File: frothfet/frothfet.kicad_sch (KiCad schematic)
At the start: 8 parts

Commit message: bom and placement all check out.  ready for production!
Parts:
- H1, H2, H3, H4: now left out of the parts list
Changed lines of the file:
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@@
 		(unit 1)
 		(exclude_from_sim no)
-		(in_bom yes)
+		(in_bom no)
 		(on_board yes)
 		(dnp no)
@@
 		(unit 1)
 		(exclude_from_sim no)
-		(in_bom yes)
+		(in_bom no)
 		(on_board yes)
 		(dnp no)
@@
 		(unit 1)
 		(exclude_from_sim no)
-		(in_bom yes)
+		(in_bom no)
 		(on_board yes)
 		(dnp no)
@@
 		(unit 1)
 		(exclude_from_sim no)
-		(in_bom yes)
-		(on_board yes)
-		(dnp no)
+		(in_bom no)
+		(on_board yes)
+		(dnp no)

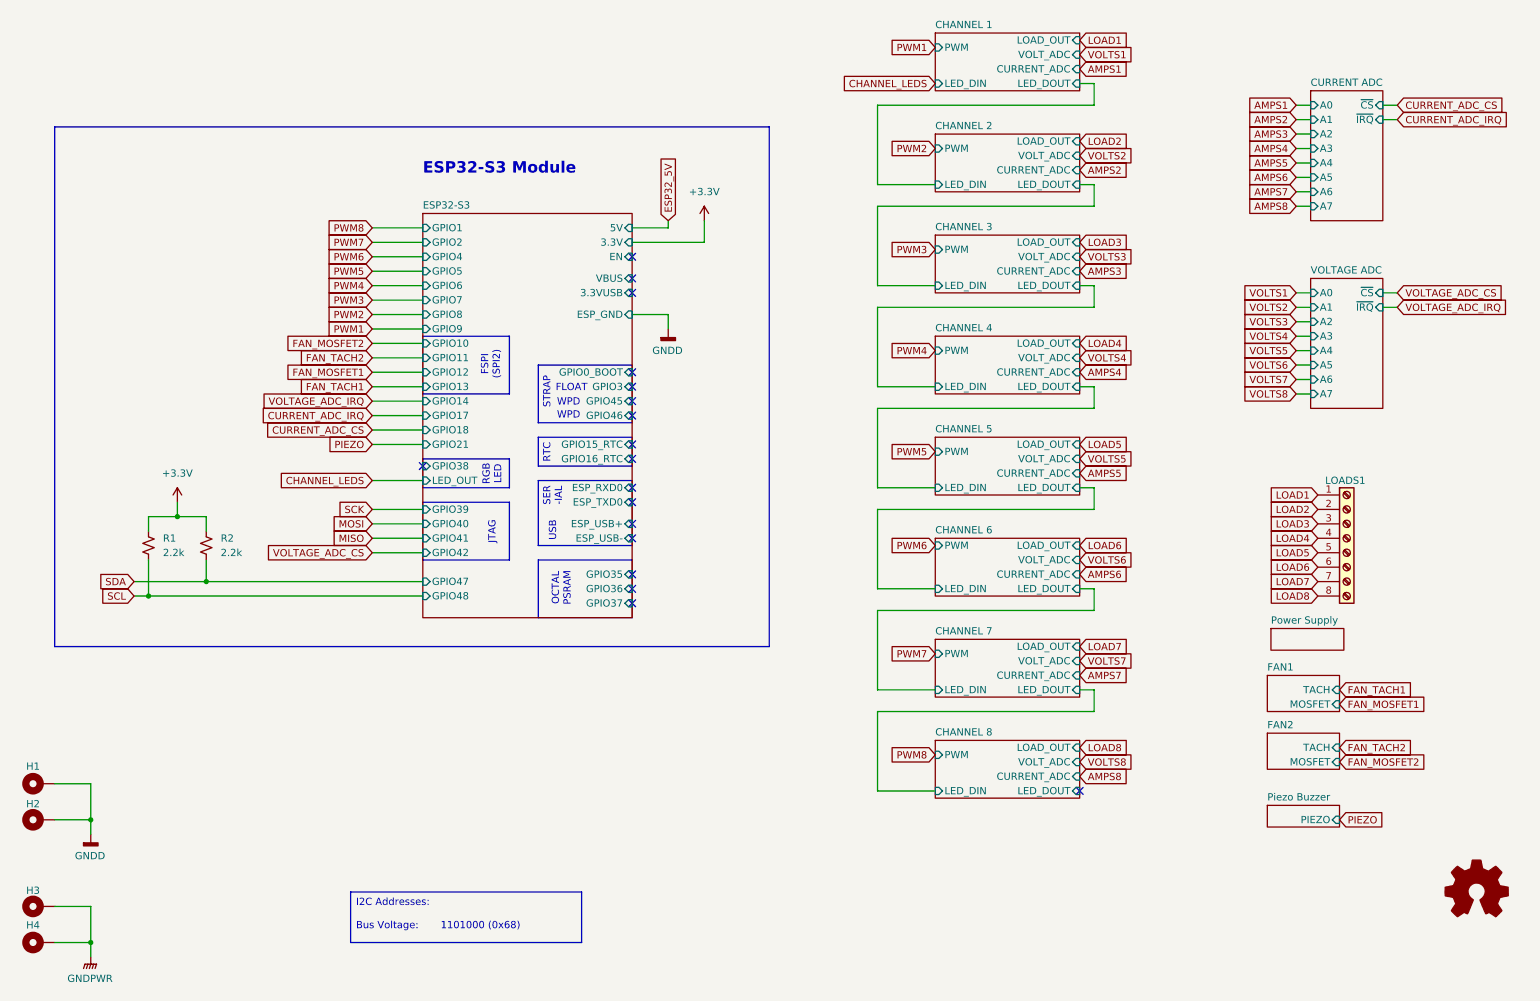
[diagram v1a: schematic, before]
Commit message: pulled in updated esp32-s3 schematic
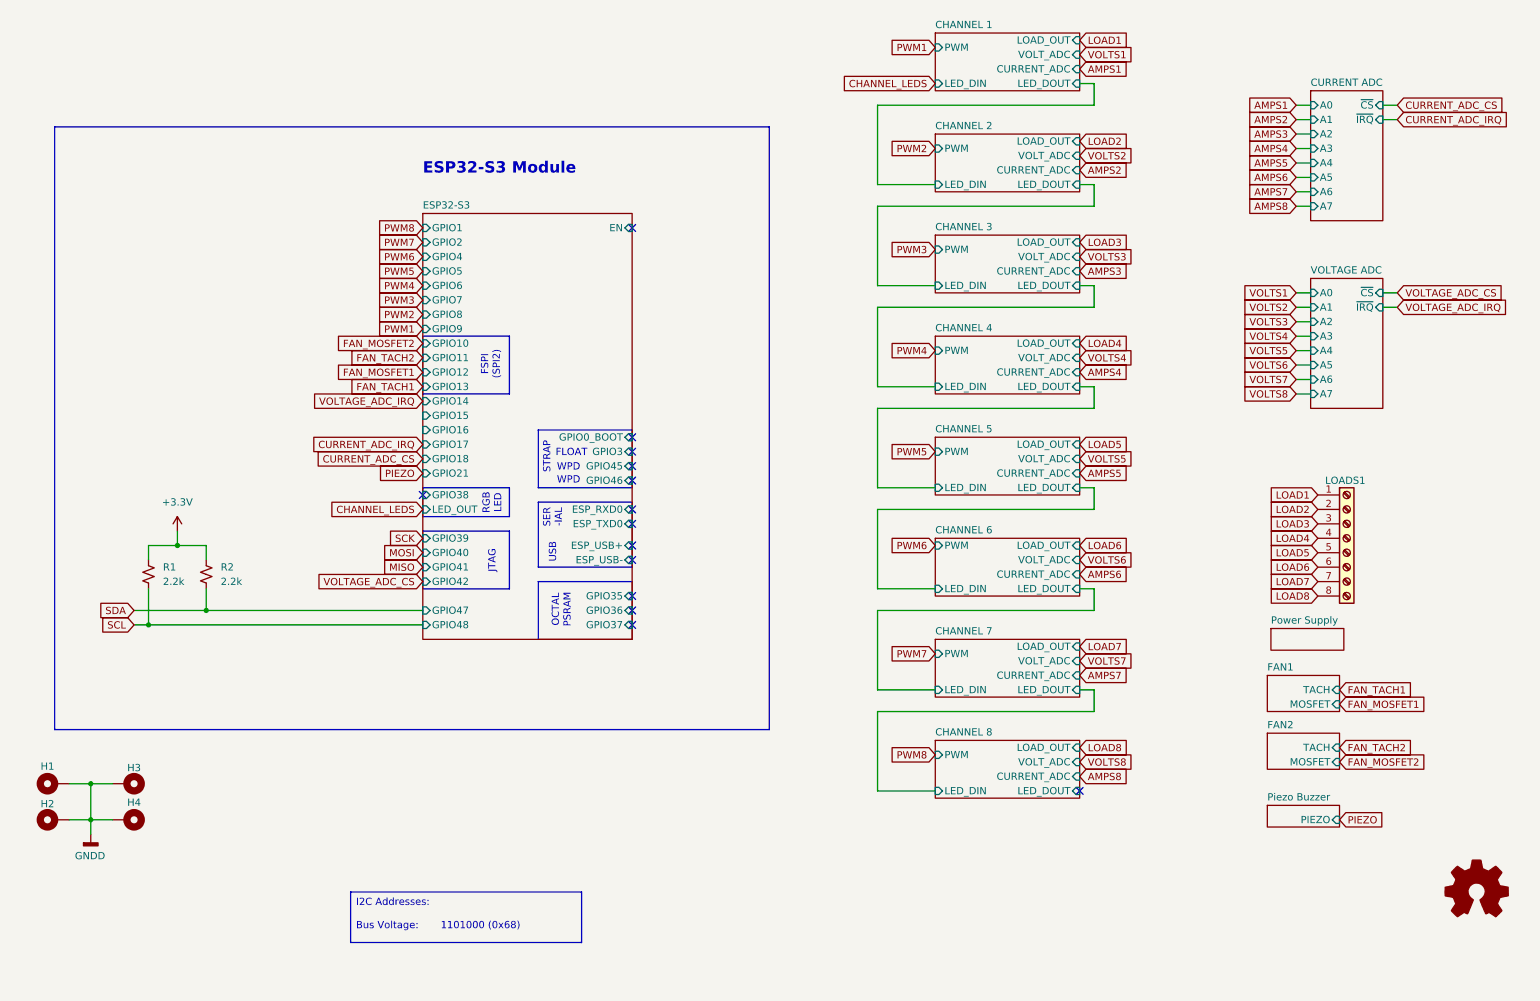
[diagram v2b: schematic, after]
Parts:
- renumbered LOGO2 to LOGO1
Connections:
- net GNDPWR is gone; now on net GNDD: H3.1, H4.1
- no-connect marks 18 -> 14
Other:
- sheet ESP32-S3 ports: added GPIO15, GPIO16; removed 3.3V, 3.3VUSB, 5V, ESP_GND, GPIO15_RTC, GPIO16_RTC, VBUS
- note removed: "RTC"
- moved on the sheet: H1, H2, H3, H4, R1, R2

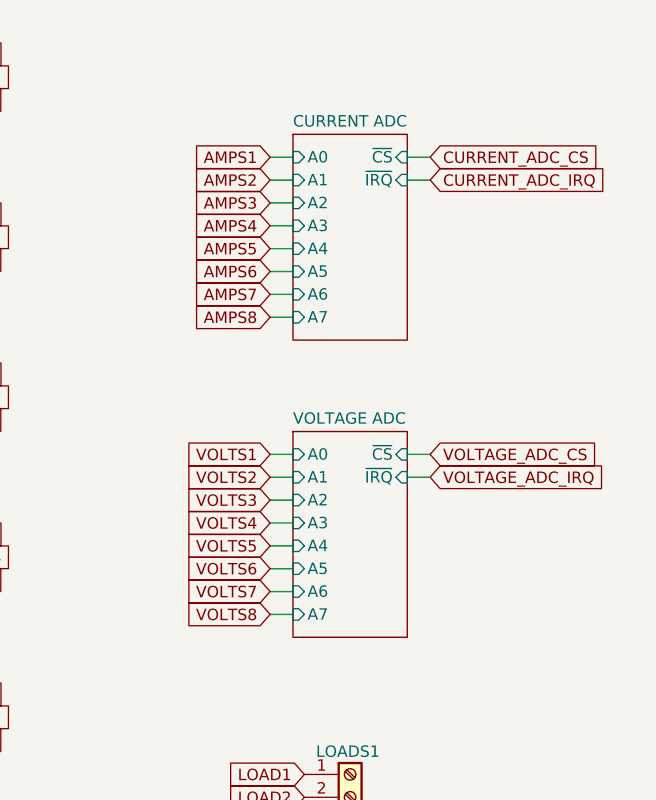
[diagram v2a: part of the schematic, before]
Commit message: removed adc and adc vref
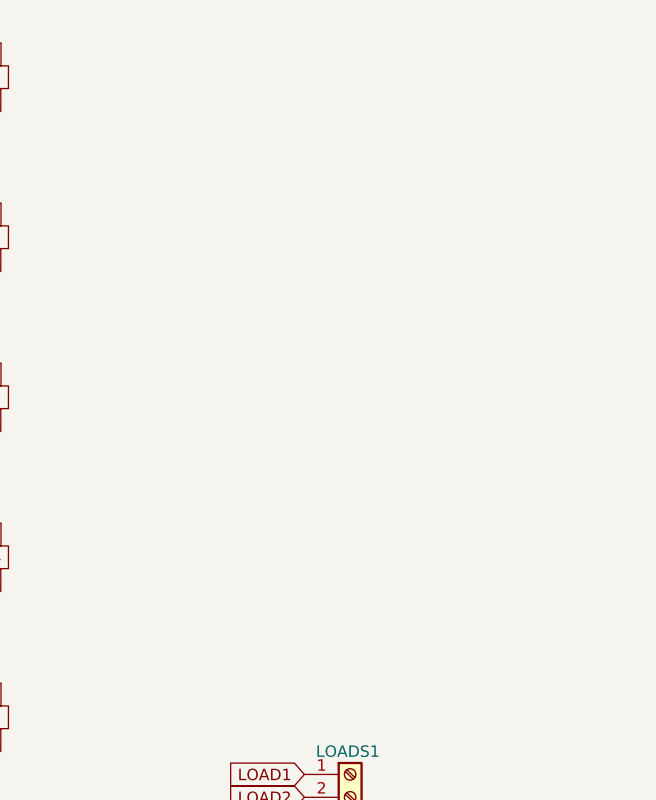
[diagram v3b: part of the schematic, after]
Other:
- removed sheet CURRENT ADC
- removed sheet VOLTAGE ADC

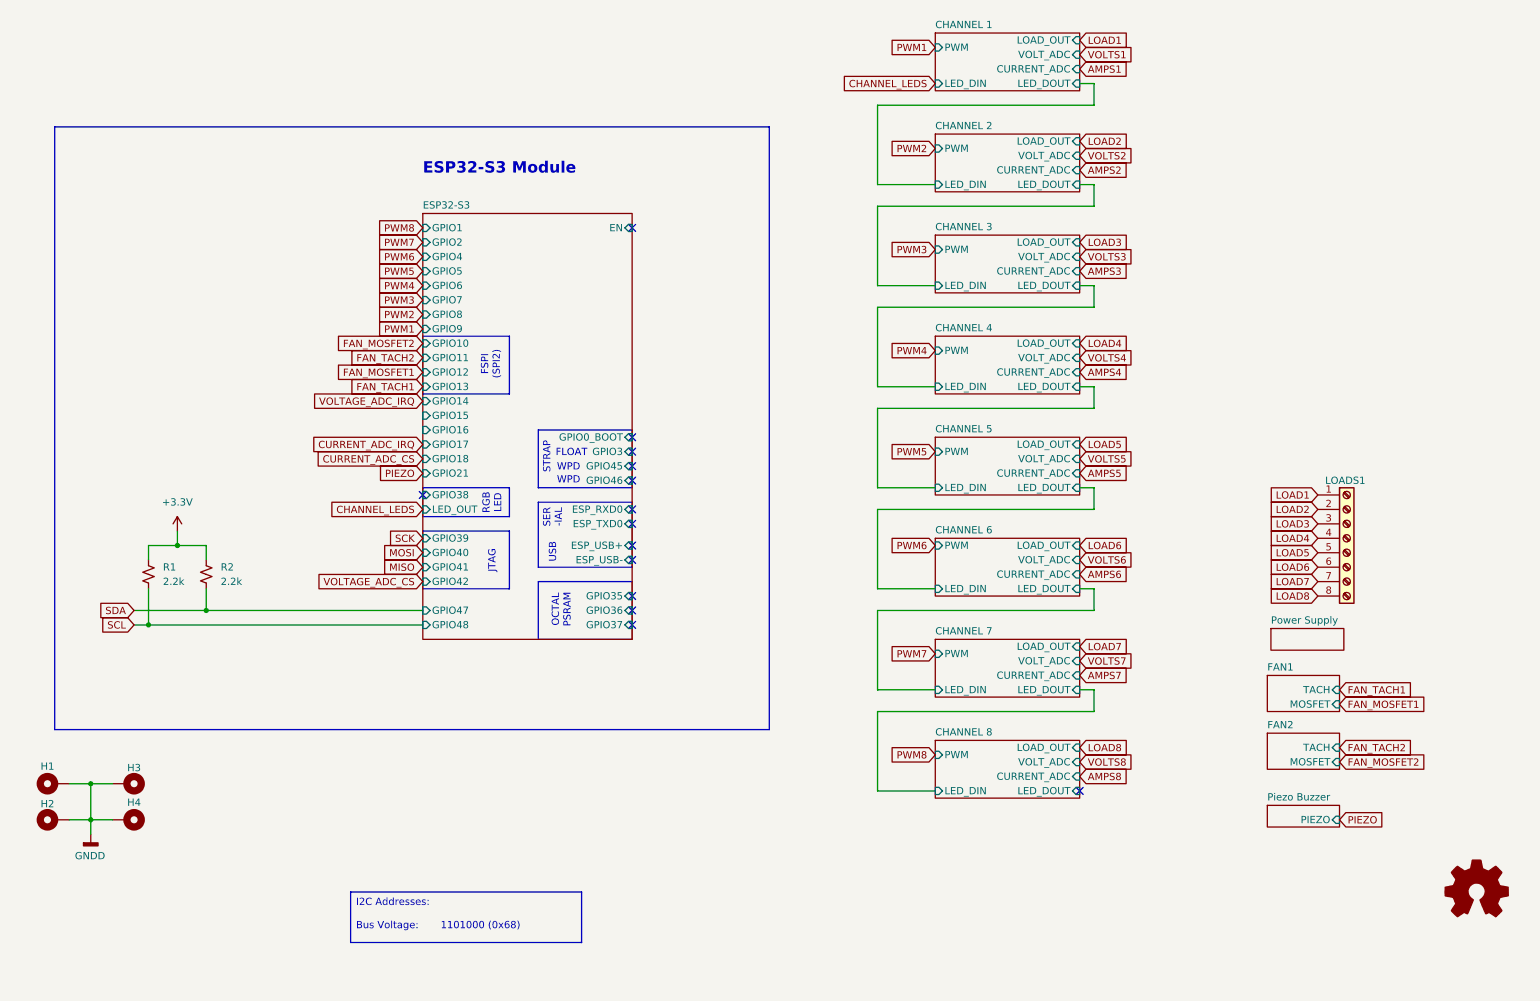
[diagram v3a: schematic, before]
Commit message: wired the i2c addresses.
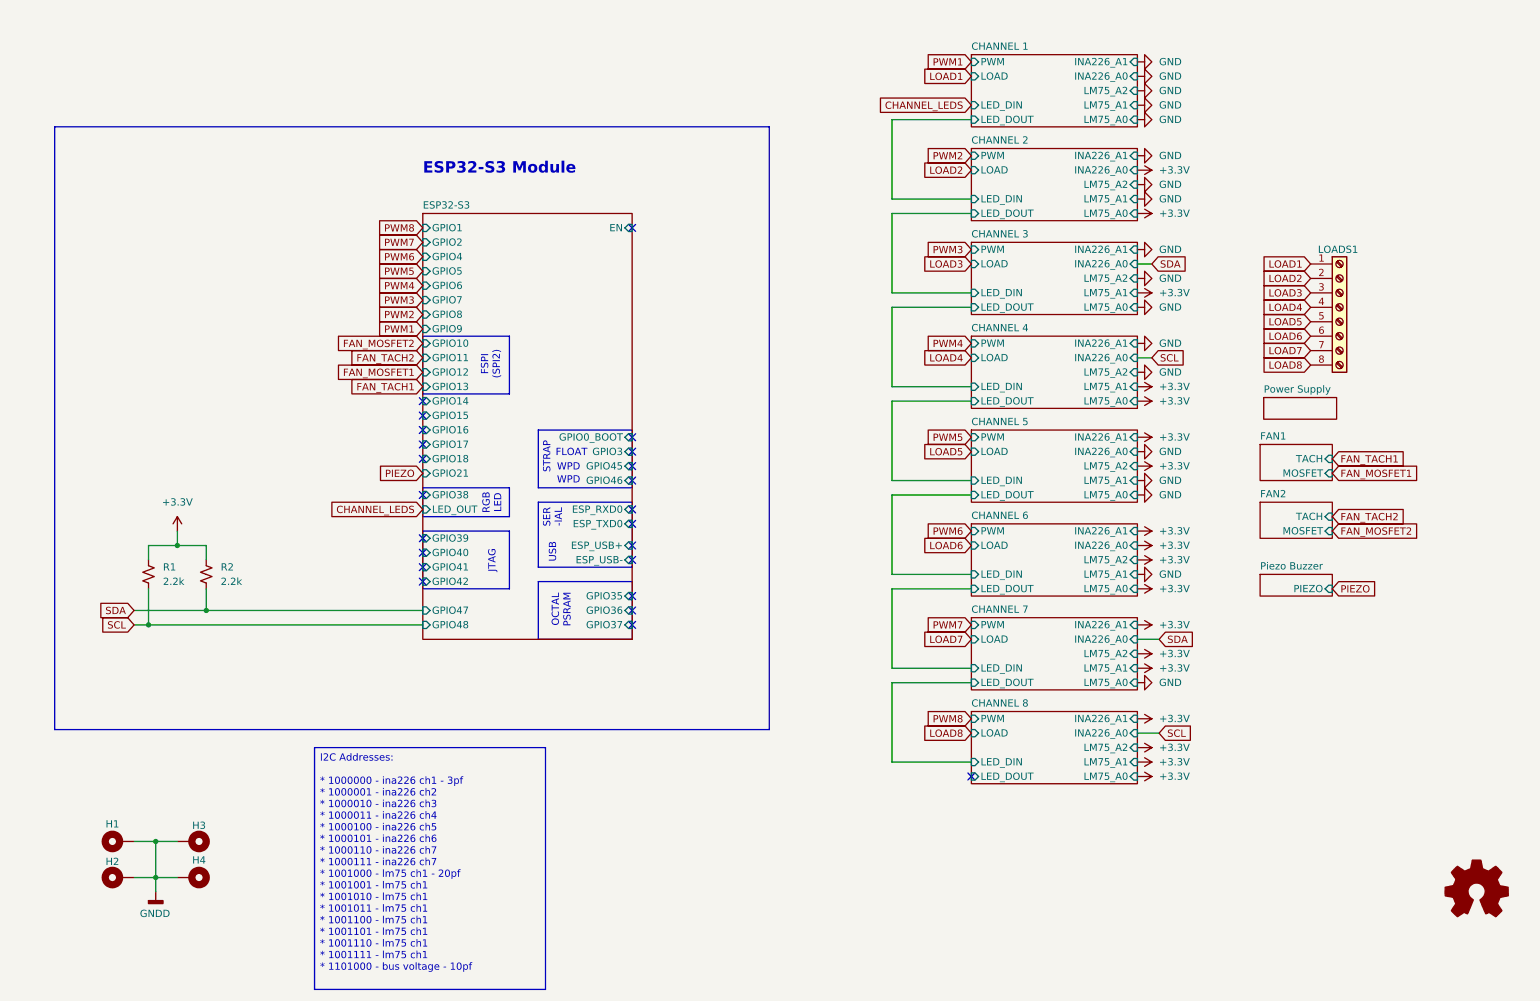
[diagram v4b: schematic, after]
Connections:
- no-connect marks 14 -> 23
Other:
- sheet CHANNEL 1 ports: added INA226_A0, INA226_A1, LM75_A0, LM75_A1, LM75_A2, LOAD; removed CURRENT_ADC, LOAD_OUT, VOLT_ADC
- sheet CHANNEL 2 ports: added INA226_A0, INA226_A1, LM75_A0, LM75_A1, LM75_A2, LOAD; removed CURRENT_ADC, LOAD_OUT, VOLT_ADC
- sheet CHANNEL 3 ports: added INA226_A0, INA226_A1, LM75_A0, LM75_A1, LM75_A2, LOAD; removed CURRENT_ADC, LOAD_OUT, VOLT_ADC
- sheet CHANNEL 4 ports: added INA226_A0, INA226_A1, LM75_A0, LM75_A1, LM75_A2, LOAD; removed CURRENT_ADC, LOAD_OUT, VOLT_ADC
- sheet CHANNEL 5 ports: added INA226_A0, INA226_A1, LM75_A0, LM75_A1, LM75_A2, LOAD; removed CURRENT_ADC, LOAD_OUT, VOLT_ADC
- sheet CHANNEL 6 ports: added INA226_A0, INA226_A1, LM75_A0, LM75_A1, LM75_A2, LOAD; removed CURRENT_ADC, LOAD_OUT, VOLT_ADC
- sheet CHANNEL 7 ports: added INA226_A0, INA226_A1, LM75_A0, LM75_A1, LM75_A2, LOAD; removed CURRENT_ADC, LOAD_OUT, VOLT_ADC
- sheet CHANNEL 8 ports: added INA226_A0, INA226_A1, LM75_A0, LM75_A1, LM75_A2, LOAD; removed CURRENT_ADC, LOAD_OUT, VOLT_ADC
- moved on the sheet: H1, H2, H3, H4, LOADS1

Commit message: added the buffer circuit
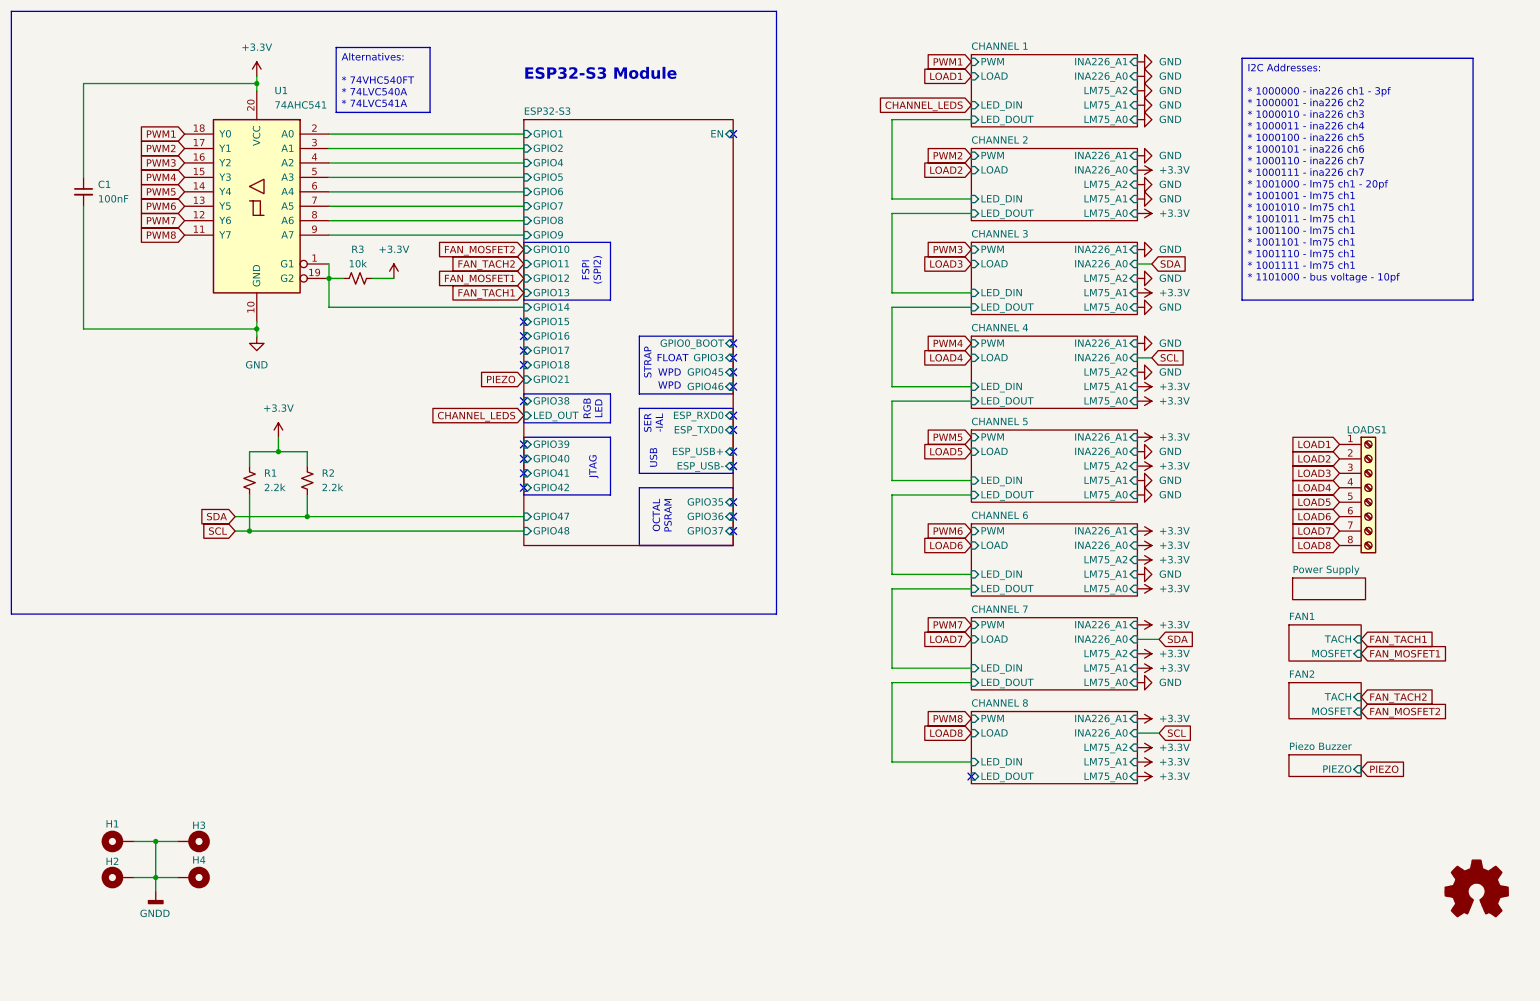
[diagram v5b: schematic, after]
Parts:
- added C1: 100nF, Capacitor_SMD:C_0603_1608Metric, symbol Device:C_Small
- added R3: 10k, Resistor_SMD:R_0603_1608Metric, symbol Device:R_Small_US
- added U1: 74AHC541, Package_SO:TSSOP-20_4.4x6.5mm_P0.65mm, symbol 74xx:74AHC541
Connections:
- net +3.3V: now also C1.1, R3.1, U1.20 (VCC)
- net ESP32-S3/GPIO14: now also R3.2, U1.1 (G1), U1.19 (G2)
- net GND: now also C1.2, U1.10 (GND)
- net PWM1: now also U1.18 (Y0)
- net PWM2: now also U1.17 (Y1)
- net PWM3: now also U1.16 (Y2)
- net PWM4: now also U1.15 (Y3)
- net PWM5: now also U1.14 (Y4)
- net PWM6: now also U1.13 (Y5)
- net PWM7: now also U1.12 (Y6)
- net PWM8: now also U1.11 (Y7)
- new net ESP32-S3/GPIO1: U1.2 (A0)
- new net ESP32-S3/GPIO2: U1.3 (A1)
- new net ESP32-S3/GPIO4: U1.4 (A2)
- new net ESP32-S3/GPIO5: U1.5 (A3)
- new net ESP32-S3/GPIO6: U1.6 (A4)
- new net ESP32-S3/GPIO7: U1.7 (A5)
- new net ESP32-S3/GPIO8: U1.8 (A6)
- new net ESP32-S3/GPIO9: U1.9 (A7)
- no-connect marks 23 -> 22
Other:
- moved on the sheet: LOADS1, R1, R2

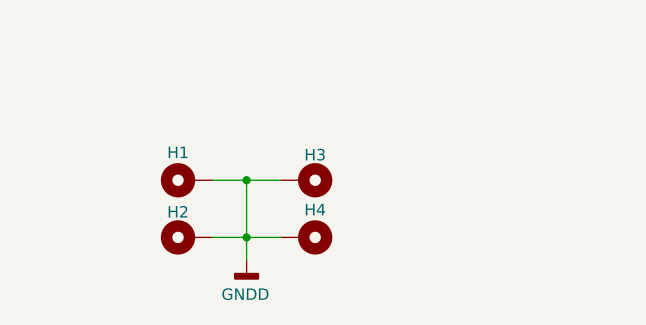
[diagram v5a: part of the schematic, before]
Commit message: changed to a single ground
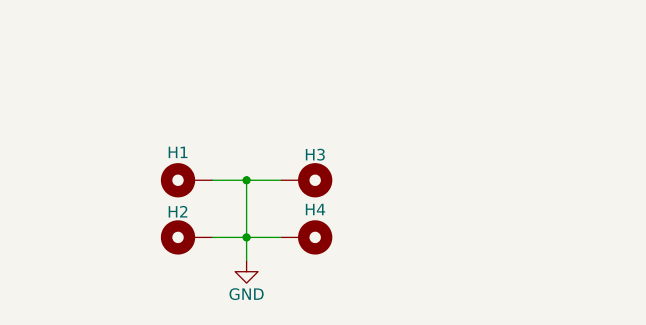
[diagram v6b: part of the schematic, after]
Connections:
- net GNDD is gone; now on net GND: H1.1, H2.1, H3.1, H4.1
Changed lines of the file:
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@@
 	)
 	(symbol
-		(lib_id "power:GNDD")
+		(lib_id "power:GND")
 		(at 43.18 173.99 0)
 		(unit 1)
@@
 		(on_board yes)
 		(dnp no)
-		(property "Reference" "#PWR01"
+		(property "Reference" "#PWR1"
 			(at 43.18 180.34 0)
 			(effects
@@
 			)
 		)
-		(property "Value" "GNDD"
-			(at 45.72 177.8 0)
+		(property "Value" "GND"
+			(at 43.18 177.8 0)
 			(effects
 				(font
 					(size 1.27 1.27)
 				)
-				(justify right)
 			)
 		)
@@
 			)
 		)
-		(property "Description" "Power symbol creates a global label with name \"GNDD\" , digital ground"
+		(property "Description" "Power symbol creates a global label with name \"GND\" , ground"
 			(at 43.18 173.99 0)
 			(effects
@@
 			(project "8ch-mosfet"
 				(path "/c83c6236-96e9-46ad-9d7a-9e2efa4a7966"
-					(reference "#PWR01")
+					(reference "#PWR1")
 					(unit 1)
 				)
